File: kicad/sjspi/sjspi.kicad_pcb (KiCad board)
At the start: 2 copper layers, 30 x 65 mm, 14 parts, among them J1 Conn_02x20_Odd_Even, J2 DB9_Female, U1 74LVC245

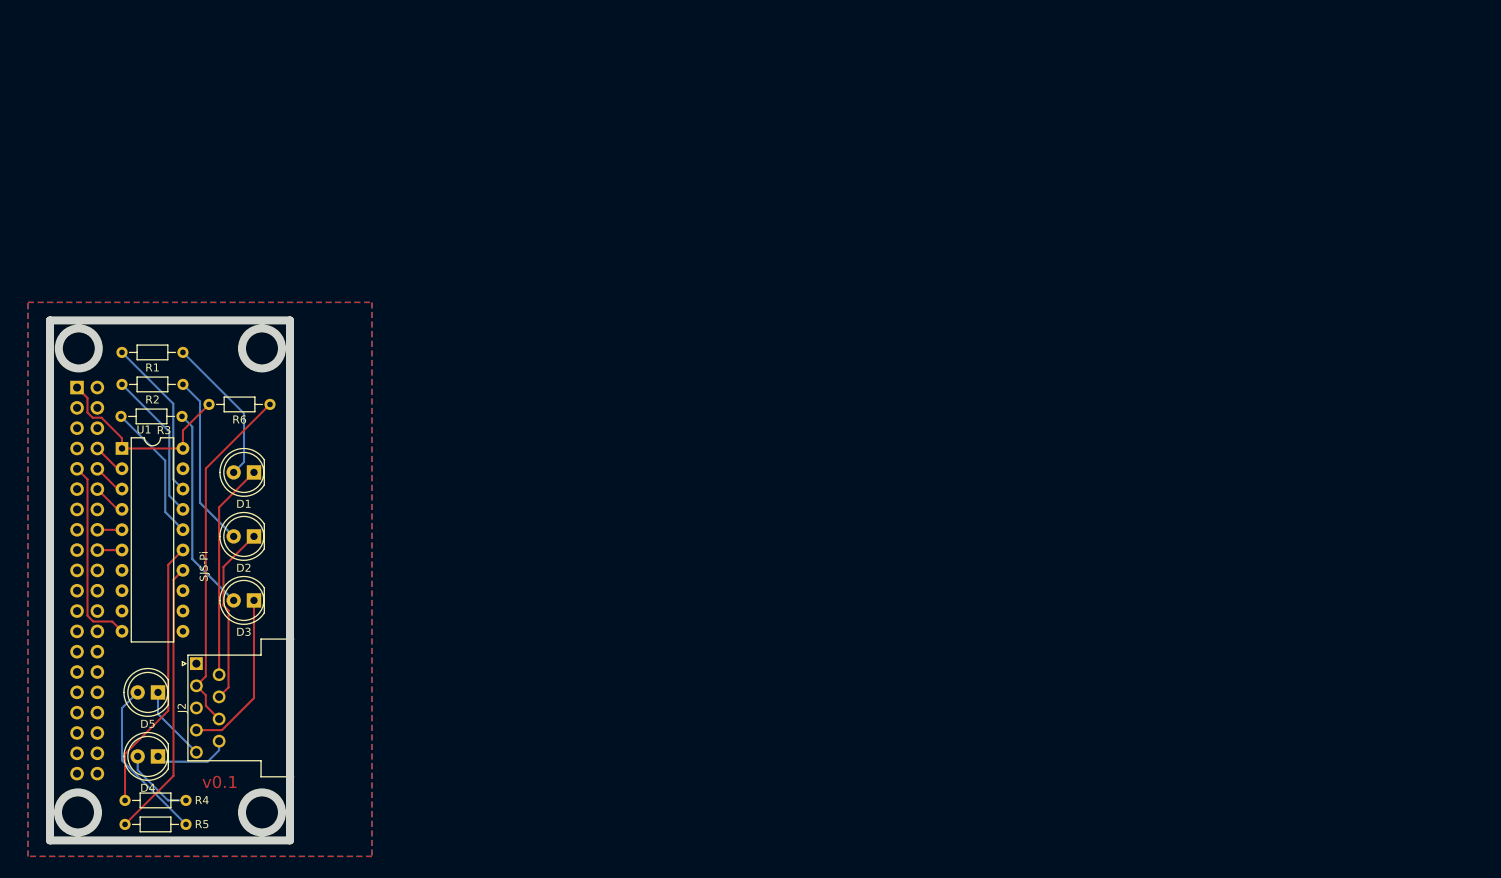
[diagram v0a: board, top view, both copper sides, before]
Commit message: v0.2 - fix pi connector position. Fix DB9 size. Connect level shifter's ground leg
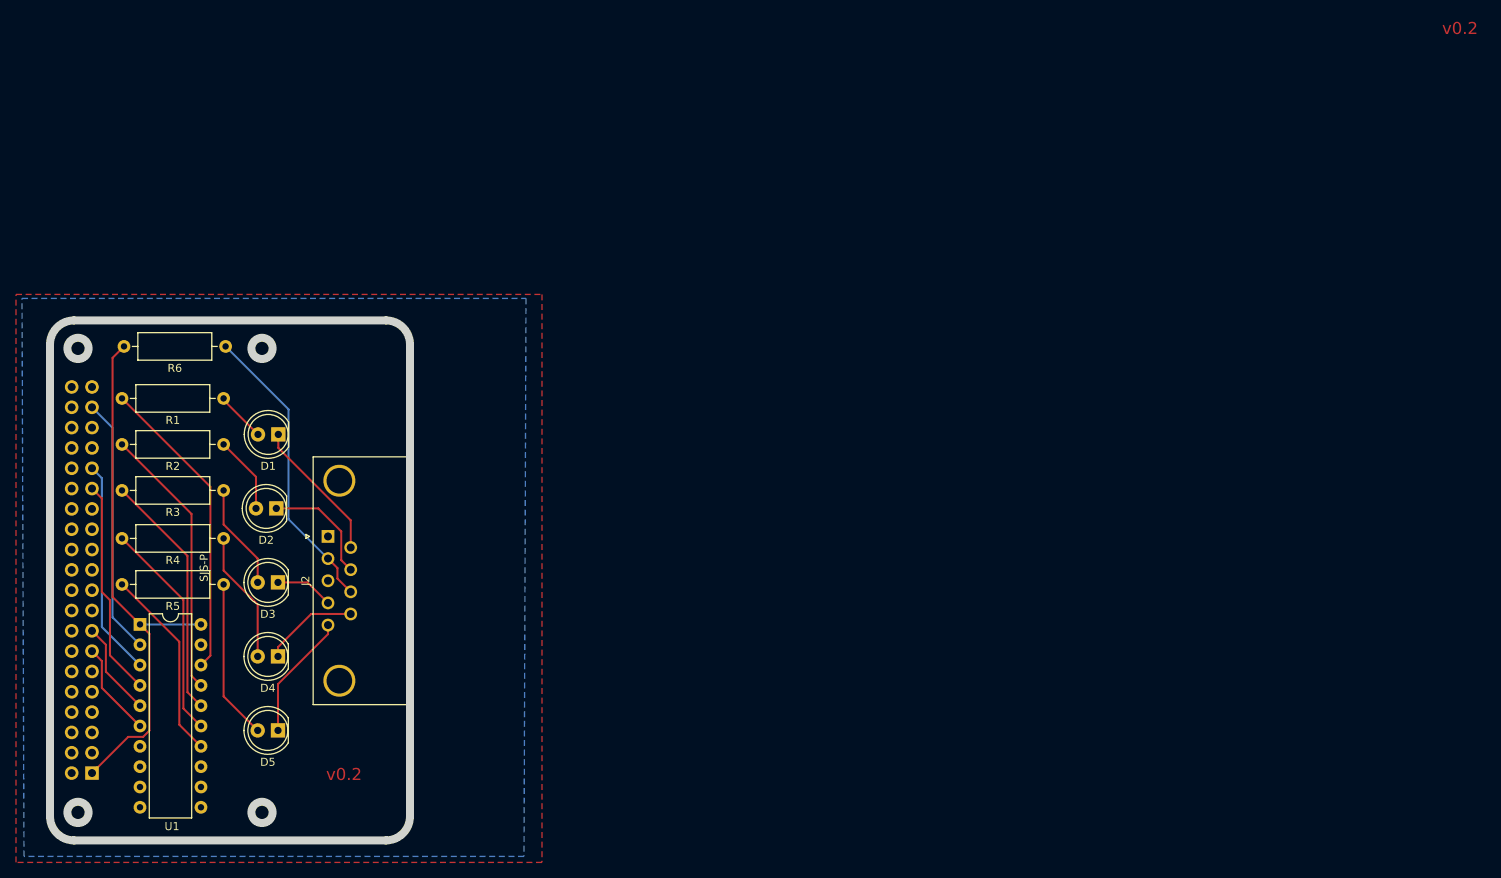
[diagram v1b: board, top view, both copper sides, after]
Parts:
- J2: footprint Connector_Dsub:DSUB-9_Female_Horizontal_P2.77x2.84mm_EdgePinOffset9.40mm -> Connector_Dsub:DSUB-9_Female_Horizontal_P2.77x2.84mm_EdgePinOffset7.70mm_Housed_MountingHolesOffset9.12mm
- R1, R2, R3, R4, R5, R6: footprint Resistor_THT:R_Axial_DIN0204_L3.6mm_D1.6mm_P7.62mm_Horizontal -> Resistor_THT:R_Axial_DIN0309_L9.0mm_D3.2mm_P12.70mm_Horizontal
- moved J1 48.2 mm to (135.2, 121.6), turned to 0 degrees
- moved R4 33.1 mm to (151.7, 92.2)
- moved R5 30.4 mm to (151.7, 98.0)
- moved J2 22.9 mm to (164.8, 92.0)
- moved U1 22.1 mm to (141.2, 103.0)
- moved D4 19.5 mm to (158.5, 107.0)
- moved D5 15.7 mm to (158.5, 116.2)
- moved R3 10.6 mm to (151.7, 86.2)
- moved R6 9.13 mm to (151.9, 68.2)
- moved R2 9.06 mm to (151.7, 80.5)
- moved R1 7.67 mm to (151.7, 74.8)
- moved D1 5.64 mm to (158.5, 79.2)
- moved D2 4.48 mm to (158.3, 88.5)
- moved D3 3.75 mm to (158.5, 97.8)
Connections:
- J1 pad 10: Net-(J1-Pad10) -> (no net)
- J1 pad 11: Net-(J1-Pad11) -> (no net)
- J1 pad 12: Net-(J1-Pad12) -> (no net)
- J1 pad 14: Net-(J1-Pad14) -> (no net)
- J1 pad 16: Net-(J1-Pad16) -> (no net)
- J1 pad 17: Net-(J1-Pad17) -> (no net)
- J1 pad 18: Net-(J1-Pad18) -> (no net)
- J1 pad 19: Net-(J1-Pad19) -> (no net)
- J1 pad 2: Net-(J1-Pad2) -> (no net)
- J1 pad 20: Net-(J1-Pad20) -> (no net)
- J1 pad 21: Net-(J1-Pad21) -> (no net)
- J1 pad 22: Net-(J1-Pad22) -> (no net)
- J1 pad 23: Net-(J1-Pad23) -> (no net)
- J1 pad 24: Net-(J1-Pad24) -> (no net)
- J1 pad 25: Net-(J1-Pad25) -> (no net)
- J1 pad 26: Net-(J1-Pad26) -> (no net)
- J1 pad 27: Net-(J1-Pad27) -> (no net)
- J1 pad 28: Net-(J1-Pad28) -> (no net)
- J1 pad 3: Net-(J1-Pad3) -> (no net)
- J1 pad 30: Net-(J1-Pad30) -> (no net)
- J1 pad 32: Net-(J1-Pad32) -> (no net)
- J1 pad 33: Net-(J1-Pad33) -> (no net)
- J1 pad 34: Net-(J1-Pad34) -> (no net)
- J1 pad 35: Net-(J1-Pad35) -> (no net)
- J1 pad 36: Net-(J1-Pad36) -> (no net)
- J1 pad 38: Net-(J1-Pad38) -> (no net)
- J1 pad 39: Net-(J1-Pad39) -> (no net)
- J1 pad 4: Net-(J1-Pad4) -> (no net)
- J1 pad 40: Net-(J1-Pad40) -> (no net)
- J1 pad 5: Net-(J1-Pad5) -> (no net)
- J1 pad 6: Net-(J1-Pad6) -> (no net)
- J1 pad 7: Net-(J1-Pad7) -> (no net)
- J1 pad 8: Net-(J1-Pad8) -> (no net)
- J2 pad 1: Net-(J2-Pad1) -> (no net)
- J2 pad 3: Net-(J2-Pad3) -> (no net)
- U1 pad 11: Net-(U1-Pad11) -> (no net)
- U1 pad 12: Net-(U1-Pad12) -> (no net)
- U1 pad 13: Net-(U1-Pad13) -> (no net)
- U1 pad 19: Net-(U1-Pad19) -> GND
- U1 pad 2: Net-(J1-Pad8) -> Net-(J1-Pad37)
- U1 pad 3: Net-(J1-Pad10) -> Net-(J1-Pad31)
- U1 pad 4: Net-(J1-Pad12) -> Net-(J1-Pad29)
- U1 pad 5: Net-(J1-Pad16) -> Net-(J1-Pad15)
- U1 pad 6: Net-(J1-Pad18) -> Net-(J1-Pad13)
- U1 pad 7: Net-(U1-Pad7) -> (no net)
- U1 pad 8: Net-(U1-Pad8) -> (no net)
- U1 pad 9: Net-(U1-Pad9) -> (no net)
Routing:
- net VCC: track 25.1 -> 67.5 mm
- net Net-(J1-Pad37): track 0.00 -> 32.2 mm
- net Net-(J1-Pad31): track 0.00 -> 27.1 mm
- net Net-(J1-Pad29): track 0.00 -> 27.1 mm
- net GND: track 24.0 -> 0.00 mm
- net Net-(R1-Pad2): track 20.2 -> 38.4 mm
- net Net-(R2-Pad2): track 18.8 -> 34.2 mm
- net Net-(D3-Pad1): track 21.1 -> 7.31 mm
- net Net-(R3-Pad2): track 17.4 -> 31.0 mm
- net Net-(D1-Pad2): track 18.7 -> 6.28 mm
- net Net-(D3-Pad2): track 25.7 -> 13.3 mm
- net Net-(D2-Pad2): track 21.6 -> 9.68 mm
- net Net-(J1-Pad15): track 0.00 -> 11.8 mm
- net Net-(J1-Pad13): track 0.00 -> 11.8 mm
- net Net-(R5-Pad2): track 34.8 -> 24.3 mm
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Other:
- board size 30 x 65 mm -> 45 x 65 mm
- board text added: "v0.2"
- board text removed: "v0.1"

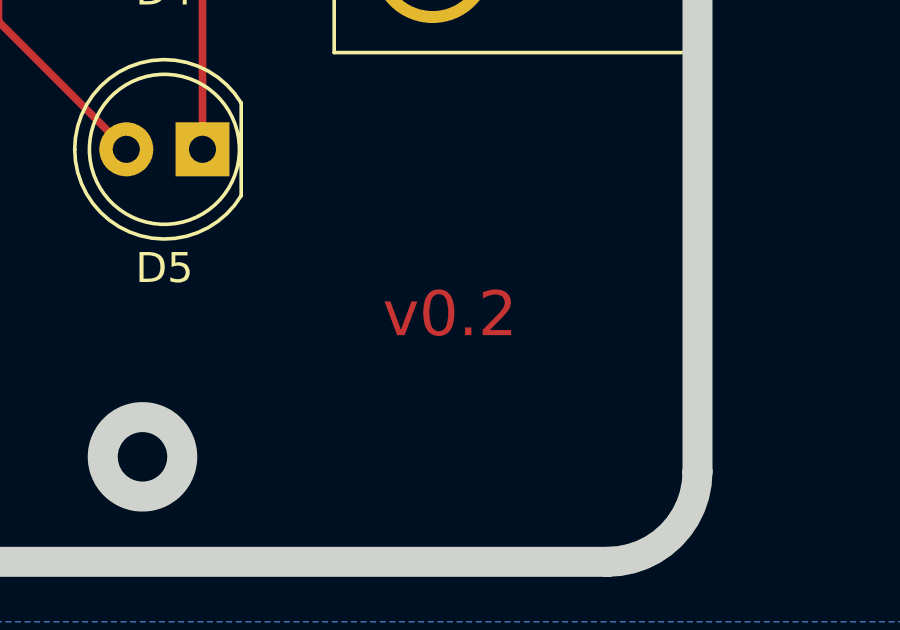
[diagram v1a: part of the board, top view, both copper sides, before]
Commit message: v0.3 - fix resistors values
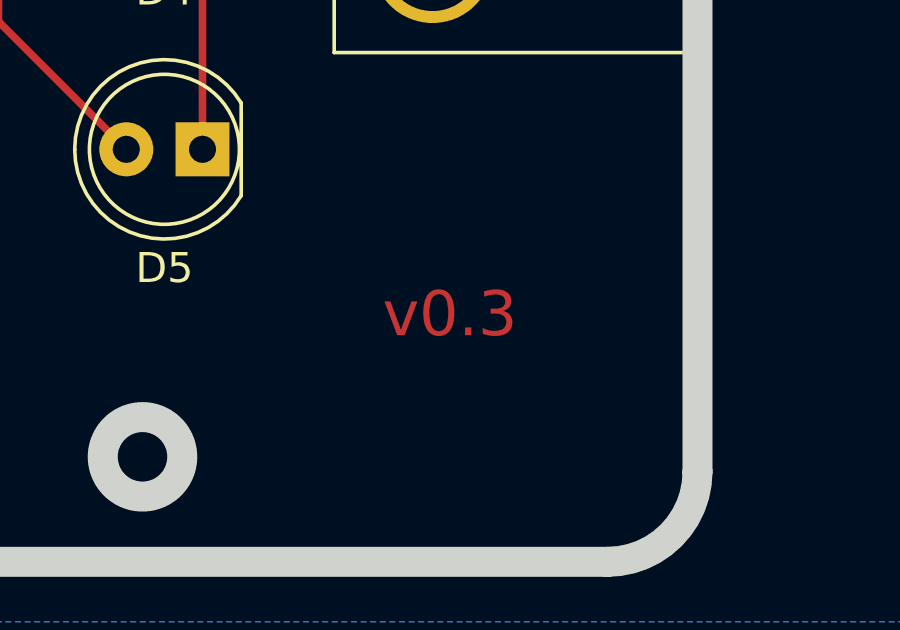
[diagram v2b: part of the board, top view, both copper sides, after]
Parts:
- R1, R2, R3, R4, R5: value 330k -> 47
- R6: value 680k -> 220
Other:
- board text added: "v0.3"

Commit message: v1.0 - Release
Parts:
- R6: value 220 -> 100
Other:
- board text added: "v1.0"
- board text removed: "v0.3"
